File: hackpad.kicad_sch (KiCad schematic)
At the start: 0 parts

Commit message: add wanted components in schematic
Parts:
- added D1, D10, D2, D3, D4, D5, D6, D7, D8, D9: 1N4148, Diode_THT:D_DO-35_SOD27_P7.62mm_Horizontal, symbol Diode:1N4148
- added J1: OLED Connection, symbol Connector:Conn_01x04_Pin
- added SW1, SW2, SW3, SW4, SW5, SW6, SW7, SW8: SW_Push, symbol Switch:SW_Push_45deg
- added SW11, SW13: RotaryEncoder_Switch, symbol Device:RotaryEncoder_Switch
- added U1: XIAO-RP2040-DIP, OPL:XIAO-RP2040-DIP, symbol OPL:XIAO-RP2040-DIP
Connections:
- new net: D1.2 (A), SW1.2
- new net: D5.2 (A), SW5.2
- new net: D4.2 (A), SW4.2
- new net: D8.2 (A), SW8.2
- new net: D3.2 (A), SW3.2
- new net: D6.2 (A), SW6.2
- new net: D7.2 (A), SW7.2
- new net: D2.2 (A), SW2.2
- new net +5V: U1.14 (VBUS)
- new net GND: J1.4 (Pin_4), U1.13 (GND)
- new net SCL: J1.2 (Pin_2)
- new net SDA: J1.1 (Pin_1)
- new net VCC: J1.3 (Pin_3)

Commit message: finish schematic
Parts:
- added D11, D12, D13, D14, D15, D16, D17, D18, D19, D20: SK6812MINI, LED_SMD:LED_SK6812MINI_PLCC4_3.5x3.5mm_P1.75mm, symbol LED:SK6812MINI
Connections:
- net +5V: now also D11.4 (VDD), D12.4 (VDD), D13.4 (VDD), D14.4 (VDD), D15.4 (VDD), D16.4 (VDD), D17.4 (VDD), D18.4 (VDD), D19.4 (VDD), D20.4 (VDD)
- net GND: now also SW11.C, SW13.C, D11.2 (VSS), D12.2 (VSS), D13.2 (VSS), D14.2 (VSS), D15.2 (VSS), D16.2 (VSS), D17.2 (VSS), D18.2 (VSS), D19.2 (VSS), D20.2 (VSS)
- net SCL: now also U1.6 (GPIO7/SCL)
- net SDA: now also U1.5 (GPIO6/SDA)
- net Column 0: now reaches SW1.1
- net Column 0: now also SW4.1, SW7.1, U1.1 (GPIO26/ADC0/A0)
- net Row 1: now reaches D5.1 (K)
- net Row 1: now also D10.1 (K), D4.1 (K), D6.1 (K)
- net Row 2: now reaches D8.1 (K)
- net Row 2: now also D7.1 (K)
- net SW11A: now reaches SW11.A
- net SW11A: now also U1.11 (GPIO3/MOSI)
- net SW11B: now reaches SW11.B
- net SW11B: now also U1.10 (GPIO4/MISO)
- net Column 3: now reaches SW11.S1
- net Column 3: now also SW13.S1, U1.4 (GPIO29/ADC3/A3)
- net SW11S2: now reaches SW11.S2
- net SW11S2: now also D9.2 (A)
- net Row 0: now reaches D9.1 (K)
- net Row 0: now also D1.1 (K), D2.1 (K), D3.1 (K)
- net Column 1: now reaches SW5.1
- net Column 1: now also SW2.1, SW8.1, U1.2 (GPIO27/ADC1/A1)
- net SW22S2: now reaches D10.2 (A)
- net SW22S2: now also SW13.S2
- net Column 2: now reaches SW3.1
- net Column 2: now also SW6.1, U1.3 (GPIO28/ADC2/A2)
- net LED: now reaches U1.7 (GPIO0/TX)
- net LED: now also D11.3 (DIN)
- net SW22B: now reaches U1.8 (GPIO1/RX)
- net SW22B: now also SW13.B
- net SW22A: now reaches U1.9 (GPIO2/SCK)
- net SW22A: now also SW13.A
- new net: D15.3 (DIN), D19.1 (DOUT)
- new net: D14.1 (DOUT), D19.3 (DIN)
- new net: D13.1 (DOUT), D14.3 (DIN)
- new net: D17.1 (DOUT), D18.3 (DIN)
- new net: D16.1 (DOUT), D17.3 (DIN)
- new net: D15.1 (DOUT), D16.3 (DIN)
- new net: D18.1 (DOUT), D20.3 (DIN)
- new net: D11.1 (DOUT), D12.3 (DIN)
- new net: D12.1 (DOUT), D13.3 (DIN)
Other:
- moved on the sheet: D1, D10, D2, D3, D4, D5, D6, D7, D8, D9, J1, SW1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

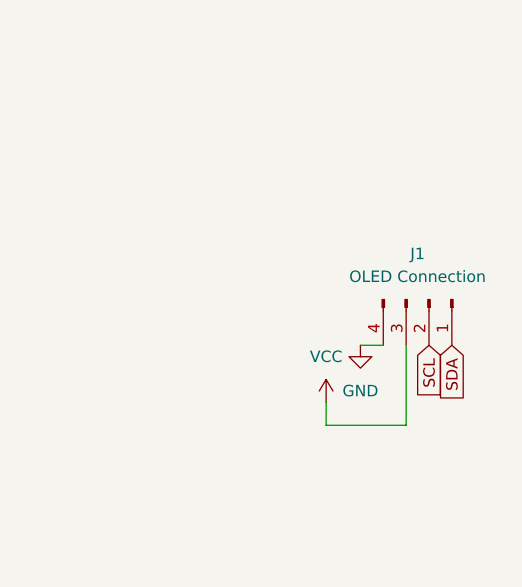
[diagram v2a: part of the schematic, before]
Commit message: place keys and OLED screen in place
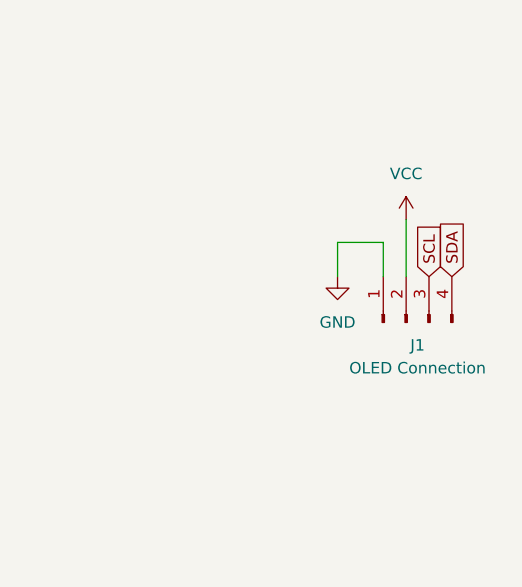
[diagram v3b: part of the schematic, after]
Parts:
- J1: footprint (none) -> OLED0.91:SSD1306-0.91-OLED-4pin-128x32
- SW1, SW2, SW3, SW4, SW5, SW6, SW7, SW8: footprint (none) -> Button_Switch_Keyboard:SW_Cherry_MX_1.00u_PCB
- SW11, SW13: footprint (none) -> Rotary_Encoder:RotaryEncoder_Alps_EC11E-Switch_Vertical_H20mm
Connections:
- net GND: now also J1.1 (Pin_1); no longer J1.4 (Pin_4)
- net SCL: now also J1.3 (Pin_3); no longer J1.2 (Pin_2)
- net SDA: now also J1.4 (Pin_4); no longer J1.1 (Pin_1)
- net VCC: now also J1.2 (Pin_2); no longer J1.3 (Pin_3)
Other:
- moved on the sheet: J1
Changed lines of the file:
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@@
 	(wire
 		(pts
-			(xy 41.91 151.13) (xy 66.04 151.13)
+			(xy 226.06 83.82) (xy 226.06 90.17)
 		)
 		(stroke
@@
 	(wire
 		(pts
-			(xy 41.91 177.8) (xy 66.04 177.8)
+			(xy 41.91 151.13) (xy 66.04 151.13)
 		)
 		(stroke
@@
 	(wire
 		(pts
-			(xy 114.3 132.08) (xy 138.43 132.08)
+			(xy 41.91 177.8) (xy 66.04 177.8)
 		)
 		(stroke
@@
 	(wire
 		(pts
-			(xy 173.99 88.9) (xy 171.45 88.9)
+			(xy 114.3 132.08) (xy 138.43 132.08)
 		)
 		(stroke
@@
 	(wire
 		(pts
-			(xy 114.3 151.13) (xy 138.43 151.13)
+			(xy 173.99 88.9) (xy 171.45 88.9)
 		)
 		(stroke
@@
 	(wire
 		(pts
-			(xy 24.13 177.8) (xy 41.91 177.8)
+			(xy 223.52 86.36) (xy 223.52 90.17)
 		)
 		(stroke
@@
 	(wire
 		(pts
-			(xy 226.06 106.68) (xy 217.17 106.68)
+			(xy 114.3 151.13) (xy 138.43 151.13)
 		)
 		(stroke
@@
 	(wire
 		(pts
-			(xy 220.98 97.79) (xy 223.52 97.79)
+			(xy 24.13 177.8) (xy 41.91 177.8)
 		)
 		(stroke
@@
 	(wire
 		(pts
-			(xy 226.06 97.79) (xy 226.06 106.68)
+			(xy 54.61 77.47) (xy 69.85 77.47)
 		)
 		(stroke
@@
 	(wire
 		(pts
-			(xy 54.61 77.47) (xy 69.85 77.47)
+			(xy 218.44 90.17) (xy 218.44 86.36)
 		)
 		(stroke
@@
 	(wire
 		(pts
+			(xy 218.44 86.36) (xy 223.52 86.36)
+		)
+		(stroke
+			(width 0)
+			(type default)
+		)
+	)
+	(wire
+		(pts
 			(xy 24.13 157.48) (xy 41.91 157.48)
 		)
@@
 	(wire
 		(pts
-			(xy 217.17 106.68) (xy 217.17 104.14)
-		)
-		(stroke
-			(width 0)
-			(type default)
-		)
-	)
-	(wire
-		(pts
 			(xy 66.04 132.08) (xy 90.17 132.08)
 		)
@@
 	(global_label "SCL"
 		(shape input)
-		(at 228.6 97.79 270)
+		(at 228.6 90.17 90)
 		(fields_autoplaced yes)
 		(effects
@@
 				(size 1.27 1.27)
 			)
-			(justify right)
+			(justify left)
 		)
 		(property "Intersheetrefs" "${INTERSHEET_REFS}"
-			(at 228.6 104.2828 90)
+			(at 228.6 83.6772 90)
 			(effects
 				(font
 					(size 1.27 1.27)
 				)
-				(justify right)
+				(justify left)
 				(hide yes)
 			)
@@
 		)
 	)
-	(global_label "SW11S2"
+	(global_label "SCL"
 		(shape input)
-		(at 154.94 54.61 0)
+		(at 135.89 107.95 180)
 		(fields_autoplaced yes)
 		(effects
@@
 				(size 1.27 1.27)
 			)
-			(justify left)
+			(justify right)
 		)
 		(property "Intersheetrefs" "${INTERSHEET_REFS}"
-			(at 165.4241 54.61 0)
+			(at 129.3972 107.95 0)
 			(effects
 				(font
 					(size 1.27 1.27)
 				)
-				(justify left)
+				(justify right)
 				(hide yes)
 			)
 		)
 	)
-	(global_label "SDA"
+	(global_label "SW11S2"
 		(shape input)
-		(at 231.14 97.79 270)
+		(at 154.94 54.61 0)
 		(fields_autoplaced yes)
 		(effects
@@
 				(size 1.27 1.27)
 			)
-			(justify right)
+			(justify left)
 		)
 		(property "Intersheetrefs" "${INTERSHEET_REFS}"
-			(at 231.14 104.3433 90)
+			(at 165.4241 54.61 0)
 			(effects
 				(font
 					(size 1.27 1.27)
 				)
-				(justify right)
+				(justify left)
 				(hide yes)
 			)
 		)
 	)
-	(global_label "SW22S2"
+	(global_label "SDA"
 		(shape input)
-		(at 191.77 54.61 0)
+		(at 231.14 90.17 90)
 		(fields_autoplaced yes)
 		(effects
@@
 		)
 		(property "Intersheetrefs" "${INTERSHEET_REFS}"
-			(at 202.2541 54.61 0)
+			(at 231.14 83.6167 90)
 			(effects
 				(font
@@
 		)
 	)
-	(global_label "SCL"
+	(global_label "SW22S2"
 		(shape input)
-		(at 135.89 107.95 180)
+		(at 191.77 54.61 0)
 		(fields_autoplaced yes)
 		(effects
@@
 				(size 1.27 1.27)
 			)
-			(justify right)
+			(justify left)
 		)
 		(property "Intersheetrefs" "${INTERSHEET_REFS}"
-			(at 129.3972 107.95 0)
+			(at 202.2541 54.61 0)
 			(effects
 				(font
 					(size 1.27 1.27)
 				)
-				(justify right)
+				(justify left)
 				(hide yes)
 			)
@@
 			)
 		)
-		(property "Footprint" ""
+		(property "Footprint" "Button_Switch_Keyboard:SW_Cherry_MX_1.00u_PCB"
 			(at 36.83 48.26 0)
 			(effects
@@
 	(symbol
 		(lib_id "power:GND")
-		(at 220.98 97.79 0)
+		(at 218.44 90.17 0)
 		(unit 1)
 		(exclude_from_sim no)
@@
 		(fields_autoplaced yes)
 		(property "Reference" "#PWR01"
-			(at 220.98 104.14 0)
+			(at 218.44 96.52 0)
 			(effects
 				(font
@@
 		)
 		(property "Value" "GND"
-			(at 220.98 102.87 0)
+			(at 218.44 95.25 0)
 			(effects
 				(font
@@
 		)
 		(property "Footprint" ""
-			(at 220.98 97.79 0)
+			(at 218.44 90.17 0)
 			(effects
 				(font
@@
 		)
 		(property "Datasheet" ""
-			(at 220.98 97.79 0)
+			(at 218.44 90.17 0)
 			(effects
 				(font
@@
 		)
 		(property "Description" "Power symbol creates a global label with name \"GND\" , ground"
-			(at 220.98 97.79 0)
+			(at 218.44 90.17 0)
 			(effects
 				(font
@@
 			)
 		)
-		(property "Footprint" ""
+		(property "Footprint" "Rotary_Encoder:RotaryEncoder_Alps_EC11E-Switch_Vertical_H20mm"
 			(at 143.51 48.006 0)
 			(effects
@@
 	(symbol
 		(lib_id "power:VCC")
-		(at 217.17 104.14 0)
+		(at 226.06 83.82 0)
 		(unit 1)
 		(exclude_from_sim no)
@@
 		(dnp no)
 		(property "Reference" "#PWR04"
-			(at 217.17 107.95 0)
+			(at 226.06 87.63 0)
 			(effects
 				(font
@@
 		)
 		(property "Value" "VCC"
-			(at 217.17 99.06 0)
+			(at 226.06 78.74 0)
 			(effects
 				(font
@@
 		)
 		(property "Footprint" ""
-			(at 217.17 104.14 0)
+			(at 226.06 83.82 0)
 			(effects
 				(font
@@
 		)
 		(property "Datasheet" ""
-			(at 217.17 104.14 0)
+			(at 226.06 83.82 0)
 			(effects
 				(font
@@
 		)
 		(property "Description" "Power symbol creates a global label with name \"VCC\""
-			(at 217.17 104.14 0)
+			(at 226.06 83.82 0)
 			(effects
 				(font
@@
 			)
 		)
-		(property "Footprint" ""
+		(property "Footprint" "Button_Switch_Keyboard:SW_Cherry_MX_1.00u_PCB"
 			(at 52.07 67.31 0)
 			(effects
@@
 			)
 		)
-		(property "Footprint" ""
+		(property "Footprint" "Button_Switch_Keyboard:SW_Cherry_MX_1.00u_PCB"
 			(at 67.31 48.26 0)
 			(effects
@@
 			)
 		)
-		(property "Footprint" ""
+		(property "Footprint" "Button_Switch_Keyboard:SW_Cherry_MX_1.00u_PCB"
 			(at 67.31 67.31 0)
 			(effects
@@
 			)
 		)
-		(property "Footprint" ""
+		(property "Footprint" "Button_Switch_Keyboard:SW_Cherry_MX_1.00u_PCB"
 			(at 36.83 67.31 0)
 			(effects
@@
 			)
 		)
-		(property "Footprint" ""
+		(property "Footprint" "Button_Switch_Keyboard:SW_Cherry_MX_1.00u_PCB"
 			(at 36.83 86.36 0)
 			(effects
@@
 	(symbol
 		(lib_id "Connector:Conn_01x04_Pin")
-		(at 228.6 92.71 270)
+		(at 226.06 95.25 90)
 		(unit 1)
 		(exclude_from_sim no)
@@
 		(fields_autoplaced yes)
 		(property "Reference" "J1"
-			(at 227.33 87.63 90)
+			(at 227.33 97.79 90)
 			(effects
 				(font
@@
 		)
 		(property "Value" "OLED Connection"
-			(at 227.33 90.17 90)
+			(at 227.33 100.33 90)
 			(effects
 				(font
@@
 			)
 		)
-		(property "Footprint" ""
-			(at 228.6 92.71 0)
+		(property "Footprint" "OLED0.91:SSD1306-0.91-OLED-4pin-128x32"
+			(at 226.06 95.25 0)
 			(effects
 				(font
@@
 		)
 		(property "Datasheet" "~"
-			(at 228.6 92.71 0)
+			(at 226.06 95.25 0)
 			(effects
 				(font
@@
 		)
 		(property "Description" "Generic connector, single row, 01x04, script generated"
-			(at 228.6 92.71 0)
+			(at 226.06 95.25 0)
 			(effects
 				(font
@@
 			)
 		)
-		(property "Footprint" ""
+		(property "Footprint" "Button_Switch_Keyboard:SW_Cherry_MX_1.00u_PCB"
 			(at 52.07 48.26 0)
 			(effects
@@
 			)
 		)
-		(property "Footprint" ""
+		(property "Footprint" "Button_Switch_Keyboard:SW_Cherry_MX_1.00u_PCB"
 			(at 52.07 86.36 0)
 			(effects
@@
 			)
 		)
-		(property "Footprint" ""
+		(property "Footprint" "Rotary_Encoder:RotaryEncoder_Alps_EC11E-Switch_Vertical_H20mm"
 			(at 180.34 48.006 0)
 			(effects
